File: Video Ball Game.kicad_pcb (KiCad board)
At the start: 2 copper layers, 250.2 x 104.1 mm, 147 parts, among them J1 RIGHT CONTROL, J10 GND, J11 GND, J12 D, J13 BL, J14 CL, J15 Video, J16 BR, J2 LEFT CONTROL, J3 FS, J4 UL, J5 NH, J6 LL, J7 GND, J8 LS, J9 GND, U1 4011, U10 4011, U11 4001, U12 4001, U13 4001, U2 4011, U3 4011, U4 4011, U5 4001, U6 4001, U7 4001, U8 4001, U9 4011

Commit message: jon's changes
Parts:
- removed S3: Power, Connector_PinHeader_2.54mm:PinHeader_1x03_P2.54mm_Vertical
- added C35: 0.1uF, Capacitor_THT:C_Disc_D3.0mm_W1.6mm_P2.50mm, F.Cu at (81.3, 57.1)
- added C36: 0.1uF, Capacitor_THT:C_Disc_D3.0mm_W1.6mm_P2.50mm, F.Cu at (81.3, 78.1)
- added C37: 0.1uF, Capacitor_THT:C_Disc_D3.0mm_W1.6mm_P2.50mm, F.Cu at (80.7, 101.6)
- added C38: 0.1uF, Capacitor_THT:C_Disc_D3.0mm_W1.6mm_P2.50mm, F.Cu at (140.4, 101.6)
- added C39: 0.1uF, Capacitor_THT:C_Disc_D3.0mm_W1.6mm_P2.50mm, F.Cu at (120.9, 67.9)
- added C40: 0.1uF, Capacitor_THT:C_Disc_D3.0mm_W1.6mm_P2.50mm, F.Cu at (144.2, 53.3)
- added C41: 0.1uF, Capacitor_THT:C_Disc_D3.0mm_W1.6mm_P2.50mm, F.Cu at (172.8, 52.7)
- added C42: 0.1uF, Capacitor_THT:C_Disc_D3.0mm_W1.6mm_P2.50mm, F.Cu at (217.8, 53.3)
- added C43: 0.1uF, Capacitor_THT:C_Disc_D3.0mm_W1.6mm_P2.50mm, F.Cu at (165.7, 105.5)
- added C44: 0.1uF, Capacitor_THT:C_Disc_D3.0mm_W1.6mm_P2.50mm, F.Cu at (165.8, 77.5)
- added C45: 0.1uF, Capacitor_THT:C_Disc_D3.0mm_W1.6mm_P2.50mm, F.Cu at (192.4, 78.7)
- added C46: 0.1uF, Capacitor_THT:C_Disc_D3.0mm_W1.6mm_P2.50mm, F.Cu at (204.5, 100.3)
- added C47: 0.1uF, Capacitor_THT:C_Disc_D3.0mm_W1.6mm_P2.50mm, F.Cu at (237.4, 74.9)
- added G***: LOGO, LOGO, F.Cu at (365.8, 131.4)
- added SW1: SW_DIP_x01, Connector_PinSocket_2.54mm:PinSocket_1x02_P2.54mm_Vertical, F.Cu at (233.7, 38.1)
- added U14: L7806, Connector_PinSocket_2.54mm:PinSocket_1x03_P2.54mm_Vertical, F.Cu at (224.8, 38.1)
- C30: value 2200 16VW -> 0.33uF; footprint Capacitor_THT:CP_Radial_D18.0mm_P7.50mm -> Capacitor_THT:C_Disc_D3.8mm_W2.6mm_P2.50mm
- C31: value 22 16VW -> 22uF 16VW
- moved C31 8.80 mm to (219.7, 42.7), turned to -90 degrees
- moved R49 7.13 mm to (220.3, 110.5), turned to 90 degrees
- moved R48 6.43 mm to (215.3, 110.5), turned to 90 degrees
- moved S1 5.08 mm to (199.4, 38.1), turned to 90 degrees
- moved C34 5.08 mm to (215.9, 118.2)
- moved C30 4.18 mm to (231.2, 45.7)
- moved J16 2.36 mm to (78.1, 51.4)
- moved J15 2.34 mm to (55.9, 118.1), turned to 0 degrees
- moved R54 1.91 mm to (109.9, 68.6)
- moved R20 1.65 mm to (64.1, 118.1)
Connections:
- net +9V renamed +6V
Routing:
- net Earth: track 54.4 -> 0.00 mm, vias 1 -> 0
- net Net-(S1-Pad1): track 94.5 -> 46.0 mm
- net Net-(S1-Pad3): track 0.00 -> 45.7 mm
- net +6V: track 609.0 -> 648.1 mm
- net Net-(BT1-Pad1): track 48.7 -> 33.7 mm
- net A: track 137.5 -> 123.9 mm
- net Net-(D7-Pad2): track 15.1 -> 19.7 mm
- net Net-(C30-Pad1): track 18.0 -> 13.9 mm
- net Net-(U10-Pad4): track 106.8 -> 103.6 mm
- net BR: track 128.9 -> 131.3 mm
- net Net-(C9-Pad2): track 45.4 -> 47.8 mm
- net Net-(C34-Pad1): track 99.5 -> 97.8 mm
- net LL: track 195.9 -> 197.5 mm, vias 9 -> 8
- net CL: track 136.3 -> 137.7 mm, vias 3 -> 2
- net Net-(R5-Pad2): track 78.2 -> 79.3 mm
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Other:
- board text added: "EA LOGO"
- board text added: "Video Ball Game David Edwards Electronics Australia May 1976"

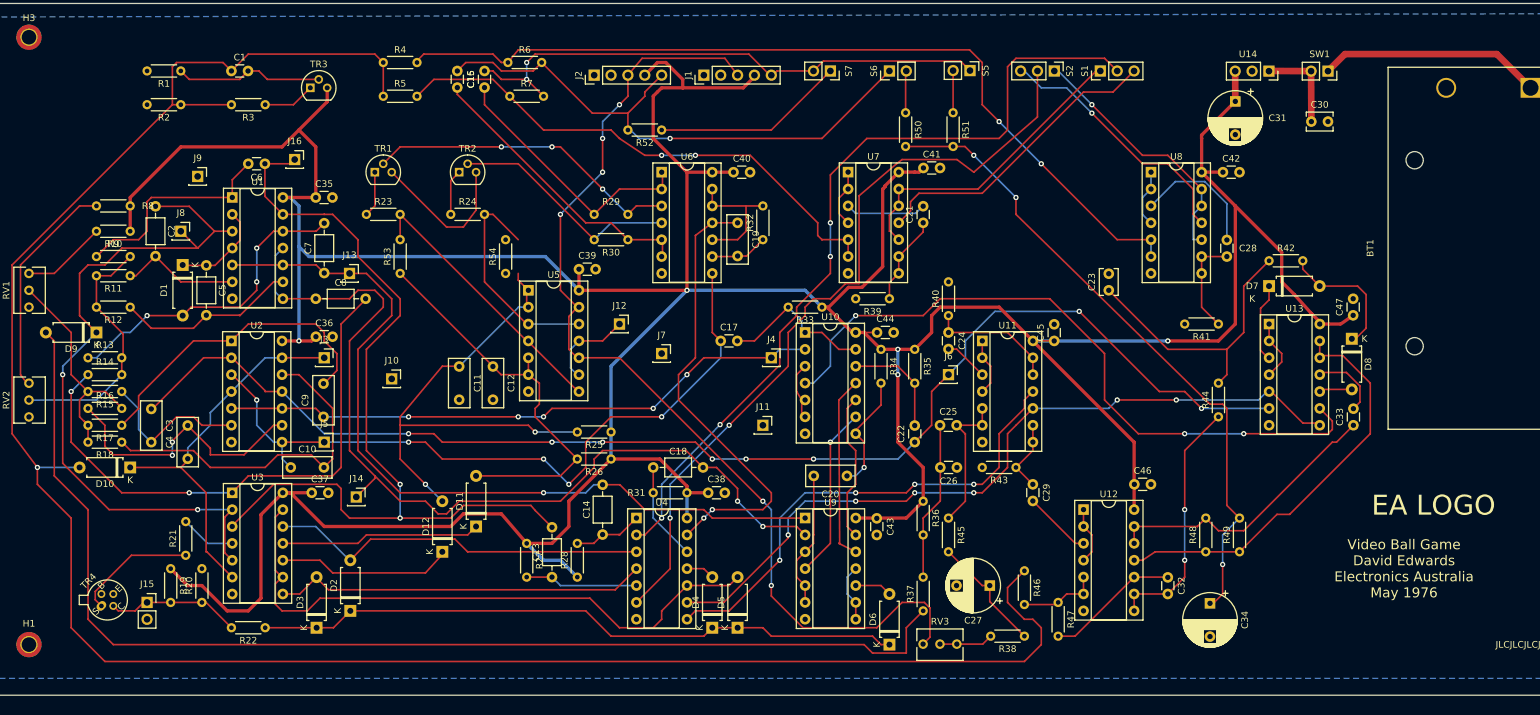
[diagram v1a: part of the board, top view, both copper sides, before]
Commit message: fixed all footprints - pcb need retracing.
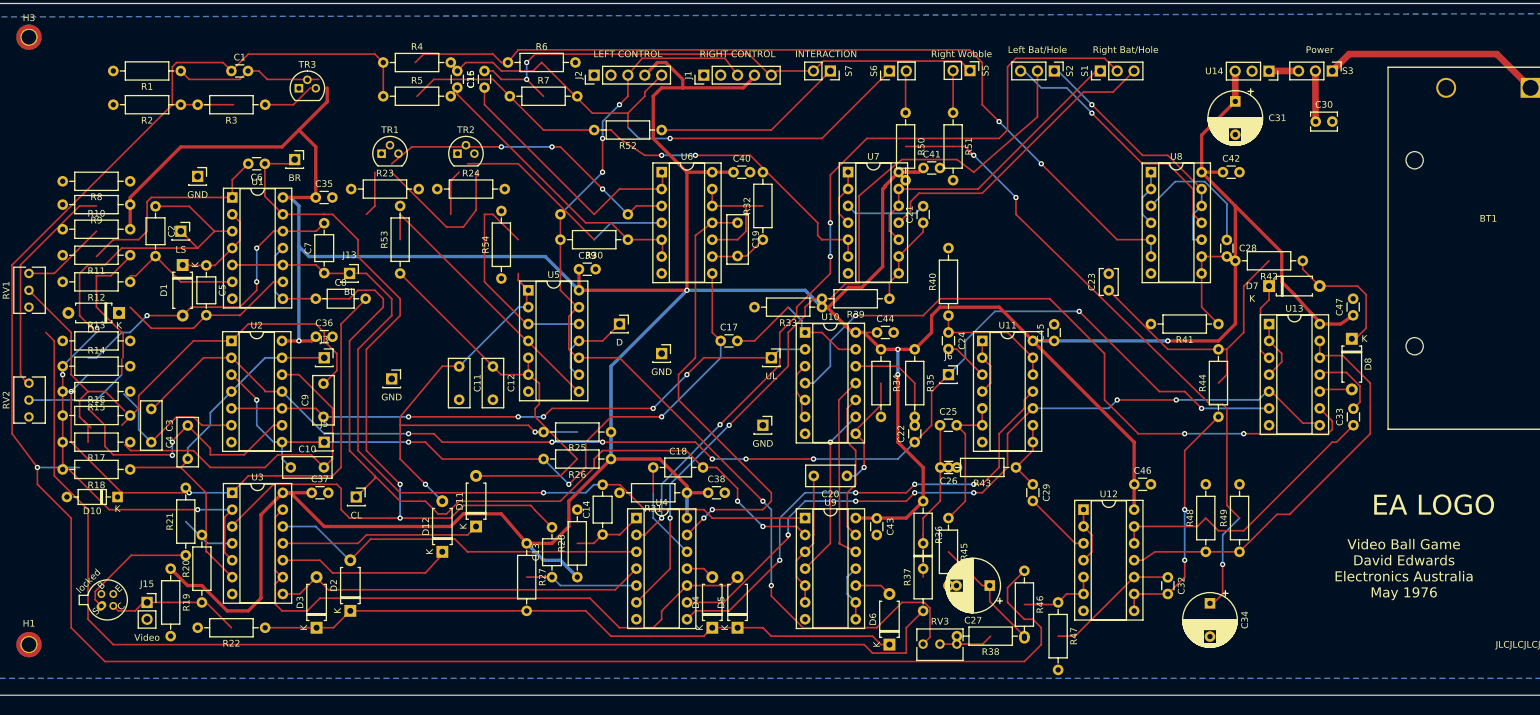
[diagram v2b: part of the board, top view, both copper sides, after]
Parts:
- removed SW1: SW_DIP_x01, Connector_PinSocket_2.54mm:PinSocket_1x02_P2.54mm_Vertical
- added S3: Power, Connector_PinHeader_2.54mm:PinHeader_1x03_P2.54mm_Vertical, F.Cu at (234.3, 38.1)
- C30: value 0.33uF -> 0.33uF -2.2uF (Jon 470uF)
- C31: value 22uF 16VW -> 22uF-100uF 16VW. Dave showed this even works with 0.5uF @17:10 on #1085
- D10: footprint Diode_THT:D_A-405_P7.62mm_Horizontal -> Diode_THT:D_DO-35_SOD27_P7.62mm_Horizontal
- R1, R10, R11, R12, R13, R14, R15, R16, R17, R18, R19, R2, R20, R21, R22, R23, R24, R25, R26, R27, R28, R29, R3, R30, R31, R32, R33, R34, R35, R36, R37, R38, R39, R4, R40, R41, R42, R43, R44, R45, R46, R47, R48, R49, R5, R50, R51, R52, R6, R7, R8, R9: footprint Resistor_THT:R_Axial_DIN0204_L3.6mm_D1.6mm_P5.08mm_Horizontal -> Resistor_THT:R_Axial_DIN0207_L6.3mm_D2.5mm_P10.16mm_Horizontal
- R53, R54: value 10M -> 10k; footprint Resistor_THT:R_Axial_DIN0204_L3.6mm_D1.6mm_P5.08mm_Horizontal -> Resistor_THT:R_Axial_DIN0207_L6.3mm_D2.5mm_P10.16mm_Horizontal
- moved R10 6.53 mm to (43.2, 61.9)
- moved D10 4.84 mm to (51.4, 102.2)
- moved R13 4.58 mm to (43.2, 78.7)
- moved D9 4.49 mm to (51.7, 74.5)
- moved R23 4.44 mm to (86.6, 55.9)
- moved R24 4.32 mm to (99.6, 55.9)
- moved R18 4.30 mm to (53.3, 98.1)
- moved R14 4.02 mm to (43.2, 82.5)
- moved R9 4.01 mm to (53.3, 58.2)
- moved R16 3.96 mm to (43.2, 90.0)
- moved R12 3.81 mm to (53.3, 69.8)
- moved R8 3.71 mm to (53.3, 54.7)
- moved R11 3.09 mm to (53.3, 65.8)
- moved TR1 2.97 mm to (91.2, 50.5)
- moved R17 2.84 mm to (53.3, 94.0)
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- renumbered TR4 to locked
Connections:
- J12 pad 1: H -> Net-(J12-Pad1)
- R53 pad 1: Net-(C12-Pad1) -> G
- R53 pad 2: F -> +6V
- R54 pad 1: Net-(C11-Pad1) -> unconnected-(R54-Pad1)
- R54 pad 2: J -> +6V
- RV3 pad 3: G -> BX
- TR1 pad 3: Net-(TR1-Pad3) -> Net-(D7-Pad2)
- TR2 pad 3: Net-(TR1-Pad3) -> Net-(D7-Pad2)
- U14 pad 1: Net-(C30-Pad1) -> Net-(S3-Pad3)
- U5 pad 10: G -> BX
- U5 pad 11: H -> Net-(J12-Pad1)
- U5 pad 13: G -> BX
- U5 pad 2: Net-(C11-Pad1) -> H
- U5 pad 5: Net-(C12-Pad1) -> G
- U5 pad 9: H -> Net-(J12-Pad1)
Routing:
- net BX: track 0.00 -> 176.8 mm, vias 0 -> 6
- net G: track 153.0 -> 0.00 mm, vias 6 -> 0
- net +6V: track 648.1 -> 765.4 mm, vias 5 -> 7
- net B: track 117.3 -> 0.00 mm, vias 2 -> 0
- net Net-(R51-Pad2): track 97.8 -> 14.5 mm
- net (no net): track 0.00 -> 83.3 mm
- net Net-(C12-Pad1): track 60.8 -> 0.00 mm
- net Net-(C11-Pad1): track 74.5 -> 135.3 mm
- net LS: track 108.3 -> 49.6 mm, vias 2 -> 0
- net Net-(C1-Pad1): track 317.5 -> 376.2 mm, vias 1 -> 3
- net Net-(R8-Pad2): track 33.8 -> 0.00 mm
- net Net-(C6-Pad2): track 32.8 -> 66.6 mm
- net Net-(R30-Pad2): track 35.0 -> 11.2 mm
- net Net-(TR1-Pad3): track 23.1 -> 0.00 mm
- net Net-(D7-Pad2): track 19.7 -> 42.8 mm
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
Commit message: USB power. removed all traces for retracing.
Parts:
- added D13: 1N4148, Diode_THT:D_DO-35_SOD27_P7.62mm_Horizontal, F.Cu at (251.0, 48.0)
- added G***: LOGO, LOGO, B.Cu at (144.5, 93.5)
- added H5: MountingHole, MountingHole:MountingHole_2.5mm_Pad, F.Cu at (37.3, 80.8)
- added H6: MountingHole, MountingHole:MountingHole_2.5mm_Pad, F.Cu at (159.8, 143.0)
- added H7: MountingHole, MountingHole:MountingHole_2.5mm_Pad, F.Cu at (153.4, 33.3)
- added H8: MountingHole, MountingHole:MountingHole_2.5mm_Pad, F.Cu at (253.5, 89.9)
- added J17: USB_B_Micro, Connector_PinHeader_2.54mm:PinHeader_1x02_P2.54mm_Vertical, F.Cu at (213.6, -17.1)
- added RV4: 4.7k, Potentiometer_THT:Potentiometer_Bourns_3266Y_Vertical, F.Cu at (65.7, 125.5)
- C1, C21, C28, C29, C32: value .01 -> 10nF red; footprint Capacitor_THT:C_Disc_D3.0mm_W1.6mm_P2.50mm -> Capacitor_THT:C_Rect_L7.2mm_W3.0mm_P5.00mm_FKS2_FKP2_MKS2_MKP2
- C10, C19, C3, C4, C9: value .01 -> 10nF red
- C11, C12: value .0047 -> 4.7nF red
- C13, C14, C18: value 100pF -> 100pF blue; footprint Capacitor_THT:C_Axial_L3.8mm_D2.6mm_P7.50mm_Horizontal -> Capacitor_THT:C_Disc_D3.0mm_W1.6mm_P2.50mm
- C15, C16, C33: value 0.1 -> 100nF red; footprint Capacitor_THT:C_Disc_D3.0mm_W1.6mm_P2.50mm -> Capacitor_THT:C_Rect_L7.2mm_W3.0mm_P5.00mm_FKS2_FKP2_MKS2_MKP2
- C17, C22: value 0.033 -> 33nF red; footprint Capacitor_THT:C_Disc_D3.0mm_W1.6mm_P2.50mm -> Capacitor_THT:C_Rect_L7.2mm_W3.0mm_P5.00mm_FKS2_FKP2_MKS2_MKP2
- C2, C5, C7, C8: value 330pF -> 330pF blue; footprint Capacitor_THT:C_Axial_L3.8mm_D2.6mm_P7.50mm_Horizontal -> Capacitor_THT:C_Disc_D5.1mm_W3.2mm_P5.00mm
- C20: value 220pF -> 220pF blue; footprint Capacitor_THT:C_Rect_L7.2mm_W3.0mm_P5.00mm_FKS2_FKP2_MKS2_MKP2 -> Capacitor_THT:C_Disc_D3.0mm_W1.6mm_P2.50mm
- C23: footprint Capacitor_THT:C_Disc_D3.8mm_W2.6mm_P2.50mm -> Capacitor_THT:CP_Radial_Tantal_D4.5mm_P5.00mm
- C24, C6: value 100pF -> 100pF blue
- C25, C26: value 330pF -> 330pF blue
- C27: value 220 16VW -> 220uF elec 16VW 8x11 mm P 3.5; footprint Capacitor_THT:CP_Radial_D8.0mm_P5.00mm -> Capacitor_THT:C_Radial_D8.0mm_H11.5mm_P3.50mm
- C30: value 0.33uF -2.2uF (Jon 470uF) -> 2200uF elec; footprint Capacitor_THT:C_Disc_D3.8mm_W2.6mm_P2.50mm -> Capacitor_THT:CP_Radial_D12.5mm_P5.00mm
- C31: value 22uF-100uF 16VW. Dave showed this even works with 0.5uF @17:10 on #1085 -> 22uF elec 16VW
- C34: value 47 16VW -> 47uF elec 16VW radial 5x11mm P2.0; footprint Capacitor_THT:CP_Radial_D8.0mm_P5.00mm -> Capacitor_THT:C_Radial_D5.0mm_H11.0mm_P2.00mm
- C35, C36, C37, C38, C39, C40, C41, C42, C43, C44, C45, C46, C47: value 0.1uF -> 100nF bypass red; footprint Capacitor_THT:C_Disc_D3.0mm_W1.6mm_P2.50mm -> Capacitor_THT:C_Rect_L7.2mm_W5.5mm_P5.00mm_FKS2_FKP2_MKS2_MKP2
- D1, D11, D12, D2, D3, D4, D5, D6, D7, D8, D9: value D -> 1N4148; footprint Diode_THT:D_A-405_P7.62mm_Horizontal -> Diode_THT:D_DO-35_SOD27_P7.62mm_Horizontal
- D10: value D -> 1N4148
- H1, H2, H3, H4: footprint MountingHole:MountingHole_2.2mm_M2_ISO14580_Pad_TopBottom -> MountingHole:MountingHole_2.5mm_Pad
- J15: footprint Connector_PinSocket_2.54mm:PinSocket_1x02_P2.54mm_Vertical -> Connector_PinHeader_2.54mm:PinHeader_1x02_P2.54mm_Vertical
- R20: value 3.3k -> 1k
- R42: value 470 -> 470k
- R50, R51, R52: footprint Resistor_THT:R_Axial_DIN0207_L6.3mm_D2.5mm_P10.16mm_Horizontal -> Library:no pads
- RV3: value 100k LIN SPEED -> 100k linear speed; footprint Potentiometer_THT:Potentiometer_Bourns_3266Y_Vertical -> Connector_PinHeader_2.54mm:PinHeader_1x03_P2.54mm_Vertical
- S3: value Power -> Power USB/9V
- S7: value INTERACTION -> Interaction; footprint Connector_PinSocket_2.54mm:PinSocket_1x02_P2.54mm_Vertical -> Connector_PinHeader_2.54mm:PinHeader_1x02_P2.54mm_Vertical
- U1, U10, U2, U3, U4, U9: value 4011 -> 4011 QUAD NAND
- U11, U12, U13, U5, U6, U7, U8: value 4001 -> 4001 QUAD NOR
- U14: footprint Connector_PinSocket_2.54mm:PinSocket_1x03_P2.54mm_Vertical -> Package_TO_SOT_THT:TO-220-3_Vertical
- moved R20 198.3 mm to (251.2, 52.3), turned to 180 degrees
- moved C46 108.4 mm to (96.8, 88.4)
- moved C44 70.5 mm to (228.6, 109.5)
- moved G*** 60.0 mm to (417.1, 100.3)
- moved C36 60.0 mm to (140.8, 70.4)
- moved J1 55.0 mm to (141.0, -16.3)
- moved J2 55.0 mm to (124.5, -16.3)
- moved R52 55.0 mm to (134.6, -8.00)
- moved S1 55.0 mm to (200.7, -16.9)
- moved S2 55.0 mm to (193.7, -16.9)
- moved S5 55.0 mm to (181.0, -17.0)
- moved S6 55.0 mm to (168.9, -16.9)
- moved S7 55.0 mm to (160.0, -16.9)
- moved C41 53.1 mm to (215.4, 84.3)
- moved R6 51.7 mm to (161.8, 40.6)
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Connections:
- H1 pad 1: (no net) -> Earth
- H2 pad 1: (no net) -> Earth
- H3 pad 1: (no net) -> Earth
- H4 pad 1: (no net) -> Earth
- R20 pad 1: VIDEO -> Net-(D13-Pad1)
- R20 pad 2: Earth -> Net-(C30-Pad1)
- TR1 pad 3: Net-(D7-Pad2) -> Net-(C23-Pad1)
- TR2 pad 3: Net-(D7-Pad2) -> Net-(C23-Pad1)
- U14 pad 1: Net-(S3-Pad3) -> Net-(C30-Pad1)
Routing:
- net +6V: track 765.4 -> 0.00 mm, vias 7 -> 0
- net Net-(C1-Pad1): track 376.2 -> 0.00 mm, vias 3 -> 0
- net LL: track 197.5 -> 0.00 mm, vias 8 -> 0
- net Net-(D9-Pad2): track 178.5 -> 0.00 mm
- net BX: track 176.8 -> 0.00 mm, vias 6 -> 0
- net CL: track 137.7 -> 0.00 mm, vias 2 -> 0
- net Net-(C11-Pad1): track 135.3 -> 0.00 mm, vias 2 -> 0
- net BR: track 131.3 -> 0.00 mm, vias 2 -> 0
- net Net-(R4-Pad2): track 130.8 -> 0.00 mm, vias 2 -> 0
- net A: track 123.9 -> 0.00 mm, vias 4 -> 0
- net BL: track 123.6 -> 0.00 mm, vias 1 -> 0
- net C: track 115.4 -> 0.00 mm, vias 6 -> 0
- net NH: track 110.4 -> 0.00 mm, vias 5 -> 0
- net Net-(U10-Pad4): track 103.6 -> 0.00 mm, vias 3 -> 0
- net Net-(D2-Pad1): track 98.2 -> 0.00 mm
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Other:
- board size 250.2 x 104.1 mm -> 226.1 x 125 mm

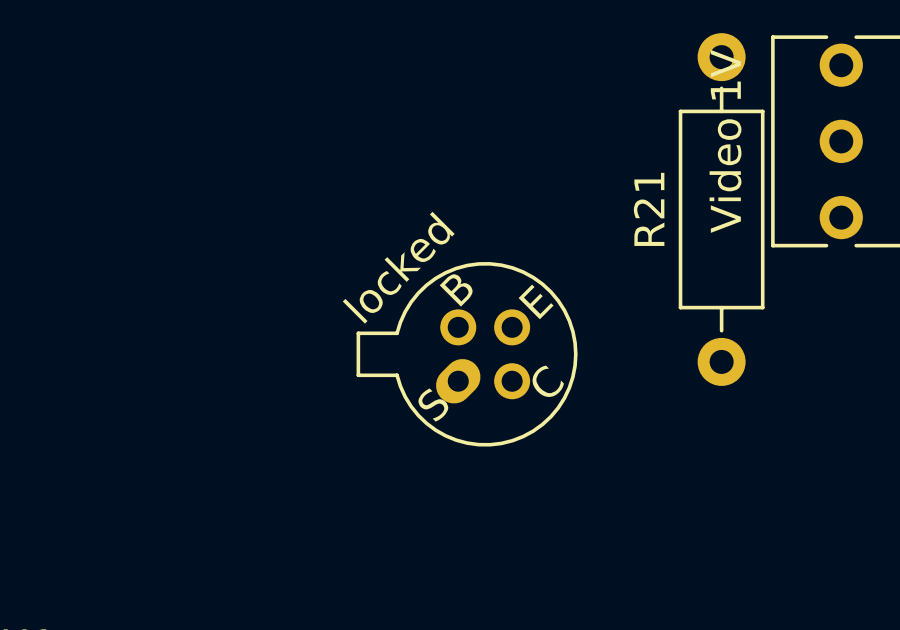
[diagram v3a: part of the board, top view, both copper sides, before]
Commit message: updated to Kicad 9.0
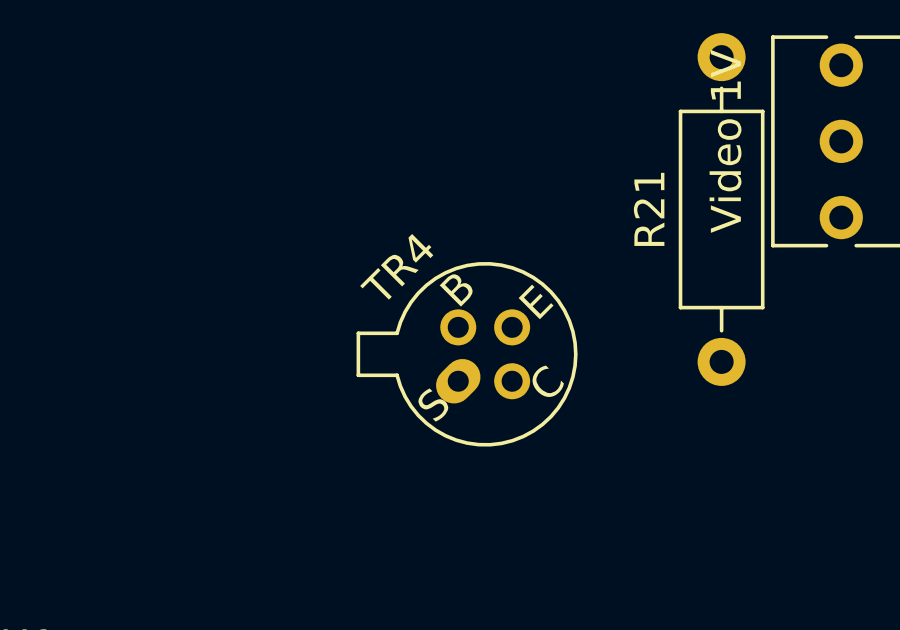
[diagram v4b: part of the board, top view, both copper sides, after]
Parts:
- renumbered locked to TR4

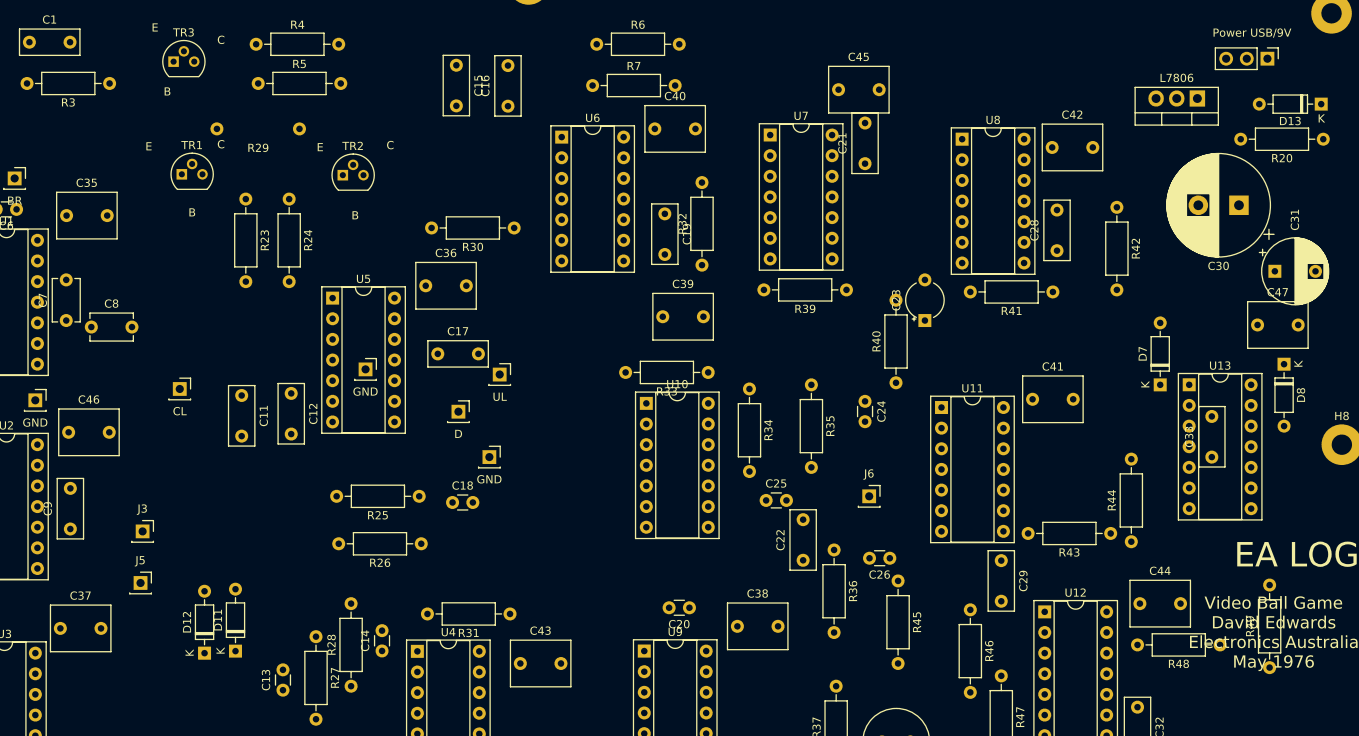
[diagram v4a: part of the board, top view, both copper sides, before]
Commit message: replaced PP with ceramic for decoupling caps
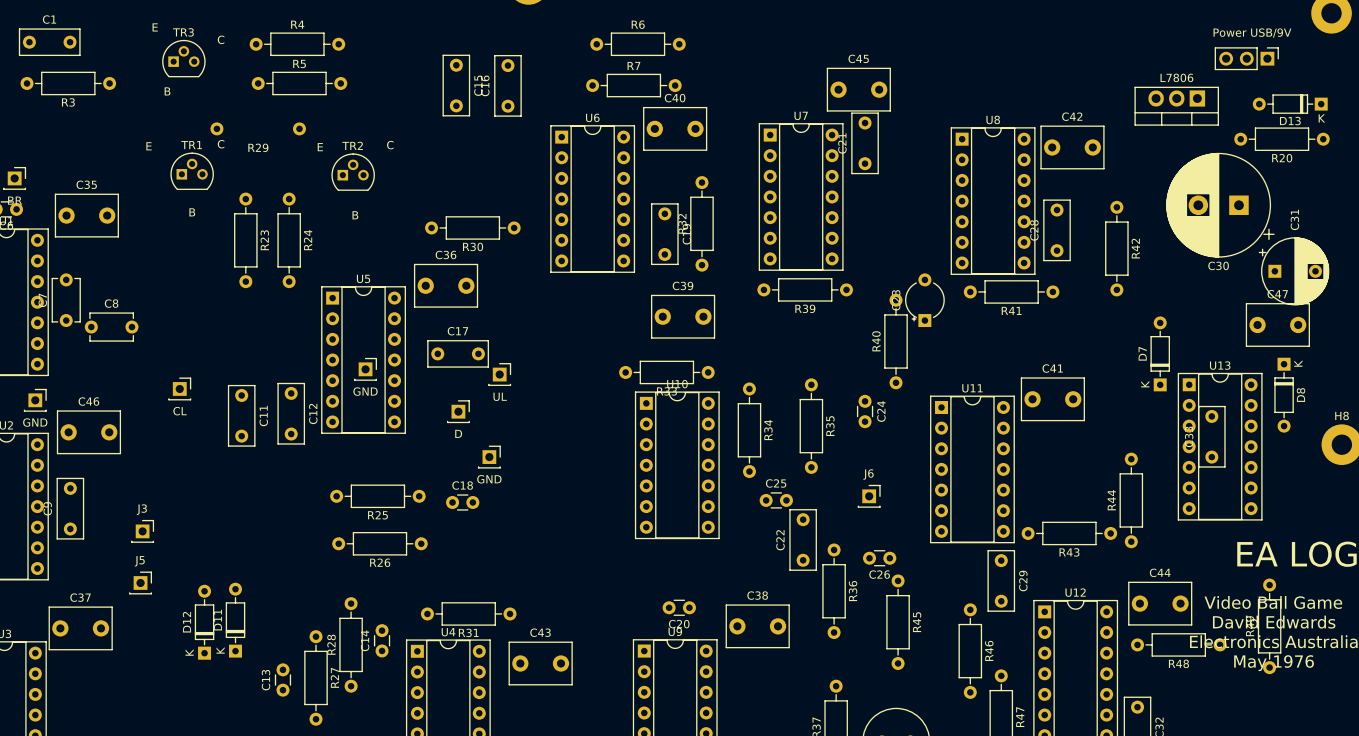
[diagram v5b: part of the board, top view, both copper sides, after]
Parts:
- C35, C36, C37, C38, C39, C40, C41, C42, C43, C44, C45, C46, C47: footprint Capacitor_THT:C_Rect_L7.2mm_W5.5mm_P5.00mm_FKS2_FKP2_MKS2_MKP2 -> Capacitor_THT:C_Disc_D7.5mm_W5.0mm_P5.00mm
